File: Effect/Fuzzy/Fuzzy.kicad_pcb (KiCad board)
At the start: 2 copper layers, 30 x 57 mm, 14 parts, among them J1 Conn_01x04_Pin, Q1 MMBFJ201

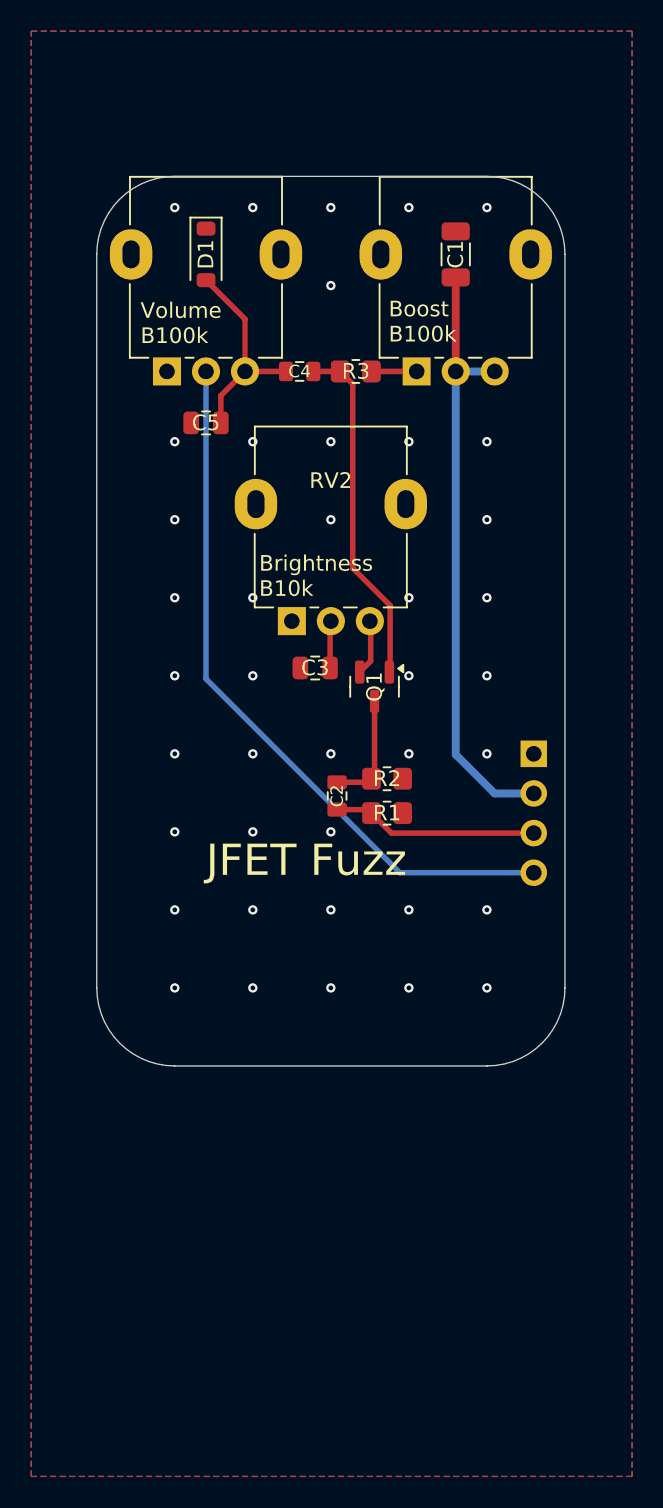
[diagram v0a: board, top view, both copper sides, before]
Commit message: First revisions from gen3 testing...
It turns out that while the single connector was sufficient, it is also
mechanically annoyingly less robust than the two separate pin headers we
used to have.

So even though we don't need the extra pins, just split it up into
"power" and a "signal" connectors again.  The placement behind the
output jack was good, so just put the power jack behind the input one
instead.

That ends up making routing nicer with the power trace going down where
it needs to be for the LED anyway, so it's a win-win.  Much nicer than
the old board.  And with the extra pins and the position right next to
the LED, lets just make the base board LED voltage available as an
"active" signal in case anybody ever wants it.

Also, just move the DC blocking capacitor and the anti-pop resistor to
ground to the base board.  Any effects board needs to do that, so it's
one less thing to worry about.  Also add back the low pass RF filter.

With the connector change, this obviously makes the new boards
incompatible, but it's not like I have any legacy boards except for the
test-boards.

On the effect board side, this does the layout changes, but also fixes
the Octaver board that was half-arsed and hadn't done proper bias
voltage calculations.  This basically just reuses them from the boost
board.

Plus use a JFET input on for the Octaver, and while at it make it also
just split the phase the natural way.  Both simpler and more balanced.

So maybe the Octaver works now.

And by "works", I obviously don't mean "sounds good".

Signed-off-by: Linus Torvalds <torvalds@linux-foundation.org>
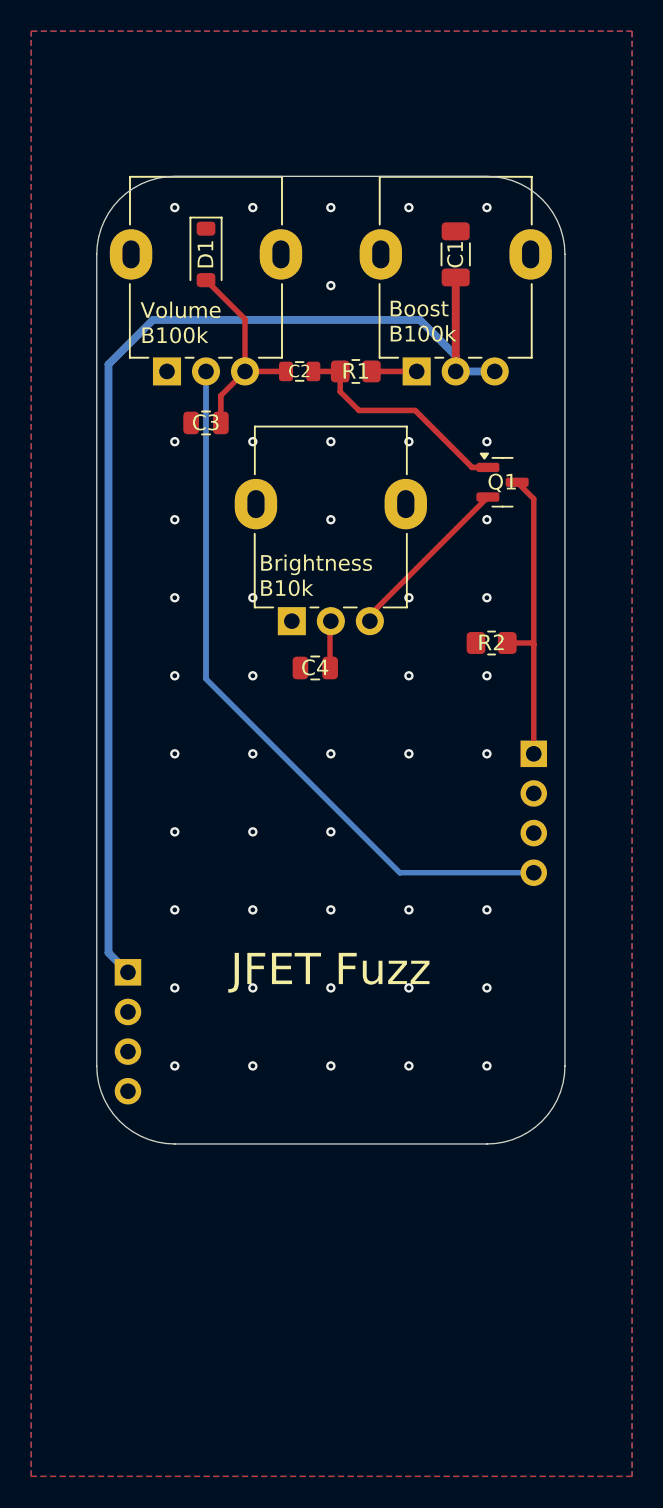
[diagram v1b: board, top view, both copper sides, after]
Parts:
- removed the C2 at (100.4, 102.7)
- removed the R1 at (103.6, 103.8)
- added J2: Conn_01x04_Pin, Connector_PinHeader_2.54mm:PinHeader_1x04_P2.54mm_Vertical, B.Cu at (87.0, 114.0)
- moved Q1 15.5 mm to (111.0, 82.6), turned to 0 degrees
- moved R2 11.0 mm to (110.3, 92.9), turned to 180 degrees
- renumbered C4 to C2, C5 to C3, C3 to C4, R3 to R1, RV3 to RV2, RV2 to RV3
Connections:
- J1 pad 1: GND -> IN
- J1 pad 2: +V -> GND
- J1 pad 3: IN -> GND
- Q1 pad 3: Net-(Q1-G) -> IN
- R2 pad 1: Net-(Q1-G) -> IN
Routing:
- net +V: track 39.1 -> 73.4 mm
- net Net-(Q1-D): track 22.3 -> 14.5 mm
- net Net-(Q1-S): track 3.57 -> 11.1 mm
- net Net-(Q1-G): track 7.02 -> 0.00 mm
- net IN: track 13.0 -> 19.6 mm
- net GND: vias 40 -> 45
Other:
- board size 30 x 57 mm -> 30 x 62 mm
